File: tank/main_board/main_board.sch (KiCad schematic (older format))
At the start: 35 parts, among them J1 PowerOut, J10 PowerMotor, J11 SigOut, J12 Spk, J13 LEDs, J14 M0, J15 M1, J16 M2, J2 PowerIn, J3 Encoder0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

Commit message: fixes
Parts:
- removed U3: SN74HC595, custom:DIP-16_W7.62mm, symbol custom:SN74HC595-custom
- added U3: SN74HC595, custom:DIP-16_W7.62mm, symbol custom:SN74HC595
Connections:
- net 4.5V: now also U3.16 (VCC)
- net GND: now also U3.13 (G), U3.8 (GND)
- net M0+: now also U3.15 (QA)
- net M0-: now also U3.1 (QB)
- net M1+: now also U3.2 (QC)
- net M1-: now also U3.3 (QD)
- net M2+: now also U3.4 (QE)
- net M2-: now also U3.5 (QF)
- net SERIAL_CLOCK: now also U3.11 (SRCLK)
- net SERIAL_DATA: now also U3.14 (SER)
- net SERIAL_LATCH: now also U3.12 (RCLK)
- net at C8.1, D1.2 (A), R1.2: now also U3.10 (SRCLR)
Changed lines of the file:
@@
 	1    0    0    -1
-$EndComp
-$Comp
-L custom:PWR_FLAG-power #FLG02
-U 1 1 59E6BC0C
-P 1350 5550
-F 0 "#FLG02" H 1350 5625 50  0001 C CNN
-F 1 "PWR_FLAG" H 1350 5700 50  0000 C CNN
-F 2 "" H 1350 5550 50  0001 C CNN
-F 3 "" H 1350 5550 50  0001 C CNN
-	1    1350 5550
-	1    0    0    -1
-$EndComp
-$Comp
-L custom:PWR_FLAG-power #FLG01
-U 1 1 59E6BD3A
-P 1200 5650
-F 0 "#FLG01" H 1200 5725 50  0001 C CNN
-F 1 "PWR_FLAG" H 1200 5800 50  0000 C CNN
-F 2 "" H 1200 5650 50  0001 C CNN
-F 3 "" H 1200 5650 50  0001 C CNN
-	1    1200 5650
-	-1   0    0    1
 $EndComp
 NoConn ~ 2400 4350
@@
 Wire Wire Line
 	6000 3850 6000 4000
-Connection ~ 1350 5550
-Connection ~ 1200 5650
 Wire Wire Line
 	6450 3300 6450 3700
@@
 Text GLabel 6650 6475 2    60   Input ~ 0
 M2-
-$Comp
-L custom:SN74HC595-custom U3
-U 1 1 5A486ACA
-P 5950 6425
-F 0 "U3" H 6100 7025 50  0000 C CNN
-F 1 "SN74HC595" H 5950 5825 50  0000 C CNN
-F 2 "custom:DIP-16_W7.62mm" H 5950 6425 50  0001 C CNN
-F 3 "" H 5950 6425 50  0001 C CNN
-	1    5950 6425
-	1    0    0    -1
-$EndComp
 Text GLabel 4100 5800 0    60   Input ~ 0
 4.5V
@@
 	3250 4600 3250 4700
 Wire Wire Line
-	1350 5550 1500 5550
-Wire Wire Line
-	1200 5650 1350 5650
-Wire Wire Line
 	5900 3750 6700 3750
 Wire Wire Line
@@
 Wire Wire Line
 	2500 5550 2650 5550
-Wire Wire Line
-	1000 5650 1200 5650
 Wire Wire Line
 	5850 4400 5850 4550
@@
 Rx
 Wire Wire Line
-	3150 6850 3450 6850
+	3150 6850 3175 6850
 Text GLabel 3450 6850 2    50   Input ~ 0
 Vm
@@
 NoConn ~ 10075 -325
 NoConn ~ 9200 4575
-$Comp
-L custom:PWR_FLAG-power #FLG0101
-U 1 1 61D3DF25
-P 3150 6850
-F 0 "#FLG0101" H 3150 6925 50  0001 C CNN
-F 1 "PWR_FLAG" H 3150 7000 50  0000 C CNN
-F 2 "" H 3150 6850 50  0001 C CNN
-F 3 "" H 3150 6850 50  0001 C CNN
-	1    3150 6850
-	1    0    0    -1
-$EndComp
-Wire Wire Line
-	950  5550 1200 5550
-Wire Wire Line
-	1200 5550 1350 5550
+Wire Wire Line
+	950  5550 1075 5550
 Connection ~ 1200 5550
 Wire Wire Line
@@
 9V
 Wire Wire Line
-	3150 6950 3450 6950
+	3150 6950 3175 6950
 Wire Wire Line
 	2200 6150 2850 6150
-$Comp
-L custom:PWR_FLAG-power #FLG0102
-U 1 1 61D3D792
-P 3150 6950
-F 0 "#FLG0102" H 3150 7025 50  0001 C CNN
-F 1 "PWR_FLAG" H 3150 7123 50  0000 C CNN
-F 2 "" H 3150 6950 50  0001 C CNN
-F 3 "~" H 3150 6950 50  0001 C CNN
-	1    3150 6950
-	1    0    0    -1
-$EndComp
-Connection ~ 3150 6950
 Text GLabel 5250 6475 0    50   Input ~ 0
 SERIAL_LATCH
@@
 Text GLabel 5850 4400 2    50   Input ~ 0
 Bump1
+Wire Wire Line
+	1200 5550 1500 5550
+Wire Wire Line
+	1000 5650 1075 5650
+$Comp
+L custom:SN74HC595 U3
+U 1 1 6202E6D3
+P 5950 6425
+F 0 "U3" H 5950 7191 50  0000 C CNN
+F 1 "SN74HC595" H 5950 7100 50  0000 C CNN
+F 2 "custom:DIP-16_W7.62mm" H 5950 6425 50  0001 C CNN
+F 3 "" H 5950 6425 50  0001 C CNN
+	1    5950 6425
+	1    0    0    -1
+$EndComp
+$Comp
+L custom:PWR_FLAG #FLG0101
+U 1 1 62037CB6
+P 1075 5550
+F 0 "#FLG0101" H 1075 5625 50  0001 C CNN
+F 1 "PWR_FLAG" H 1075 5723 50  0000 C CNN
+F 2 "" H 1075 5550 50  0001 C CNN
+F 3 "" H 1075 5550 50  0001 C CNN
+	1    1075 5550
+	1    0    0    -1
+$EndComp
+Connection ~ 1075 5550
+Wire Wire Line
+	1075 5550 1200 5550
+$Comp
+L custom:PWR_FLAG #FLG0102
+U 1 1 62038348
+P 1075 5650
+F 0 "#FLG0102" H 1075 5725 50  0001 C CNN
+F 1 "PWR_FLAG" H 1075 5823 50  0000 C CNN
+F 2 "" H 1075 5650 50  0001 C CNN
+F 3 "" H 1075 5650 50  0001 C CNN
+	1    1075 5650
+	-1   0    0    1
+$EndComp
+Connection ~ 1075 5650
+Wire Wire Line
+	1075 5650 1350 5650
+$Comp
+L custom:PWR_FLAG #FLG0103
+U 1 1 620389A9
+P 3175 6850
+F 0 "#FLG0103" H 3175 6925 50  0001 C CNN
+F 1 "PWR_FLAG" H 3175 7023 50  0000 C CNN
+F 2 "" H 3175 6850 50  0001 C CNN
+F 3 "" H 3175 6850 50  0001 C CNN
+	1    3175 6850
+	1    0    0    -1
+$EndComp
+Connection ~ 3175 6850
+Wire Wire Line
+	3175 6850 3450 6850
+$Comp
+L custom:PWR_FLAG #FLG0104
+U 1 1 62038DED
+P 3175 6950
+F 0 "#FLG0104" H 3175 7025 50  0001 C CNN
+F 1 "PWR_FLAG" H 3175 7123 50  0000 C CNN
+F 2 "" H 3175 6950 50  0001 C CNN
+F 3 "" H 3175 6950 50  0001 C CNN
+	1    3175 6950
+	-1   0    0    1
+$EndComp
+Connection ~ 3175 6950
+Wire Wire Line
+	3175 6950 3450 6950
 $EndSCHEMATC

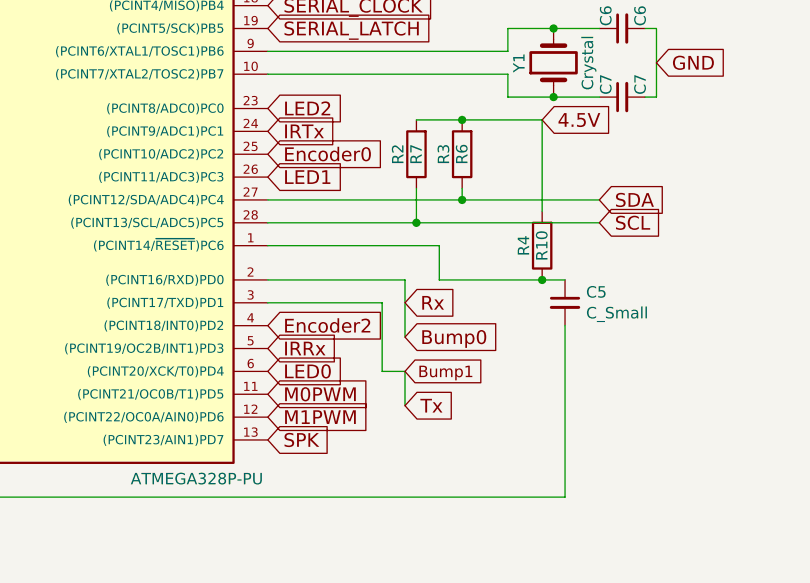
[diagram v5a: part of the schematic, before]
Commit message: Version 0.11: - Better labelling - Put LED output on Rx and Tx pins. This way, we won't be attaching interrutps to Serial pins
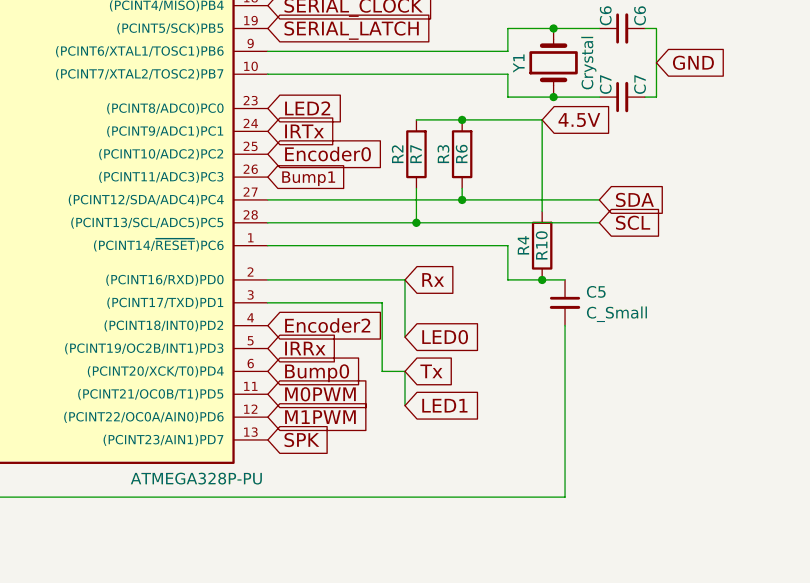
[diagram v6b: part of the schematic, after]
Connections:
- net Bump0: now also U2.6 ((PCINT20/XCK/T0)PD4); no longer J9.4 (Pin_4), U2.2 ((PCINT16/RXD)PD0)
- net Bump1: now also U2.26 ((PCINT11/ADC3)PC3); no longer J9.5 (Pin_5), U2.3 ((PCINT17/TXD)PD1)
- net LED0: now also J9.4 (Pin_4), U2.2 ((PCINT16/RXD)PD0); no longer U2.6 ((PCINT20/XCK/T0)PD4)
- net LED1: now also J9.5 (Pin_5), U2.3 ((PCINT17/TXD)PD1); no longer U2.26 ((PCINT11/ADC3)PC3)
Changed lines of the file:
@@
 Connection ~ 3250 4600
-Wire Wire Line
-	5250 3850 6000 3850
-Wire Wire Line
-	6000 4000 6450 4000
-Wire Wire Line
-	6000 3850 6000 4000
 Wire Wire Line
 	6450 3300 6450 3700
@@
 Text GLabel 2050 3500 2    60   Input ~ 0
 GND
-Text GLabel 5250 4400 2    60   Input ~ 0
+Text GLabel 5850 4250 2    60   Input ~ 0
 LED0
-Text GLabel 5250 3550 2    60   Input ~ 0
+Text GLabel 5850 4550 2    60   Input ~ 0
 LED1
 Text GLabel 6450 3300 2    60   Input ~ 0
@@
 Text GLabel 6950 3050 2    60   Input ~ 0
 GND
-Connection ~ 6450 4000
 Text GLabel 3150 950  0    60   Input ~ 0
 IRTx
@@
 Wire Wire Line
 	5750 4400 5850 4400
-Text GLabel 5850 4250 2    60   Input ~ 0
+Text GLabel 5250 4400 2    60   Input ~ 0
 Bump0
 Text GLabel 5500 1800 0    60   Input ~ 0
@@
 Wire Wire Line
 	5850 4400 5850 4550
-Text GLabel 5850 4550 2    60   Input ~ 0
+Text GLabel 5850 4400 2    60   Input ~ 0
 Tx
-Text GLabel 5850 4100 2    60   Input ~ 0
+Text GLabel 5850 4000 2    60   Input ~ 0
 Rx
 Wire Wire Line
@@
 Wire Wire Line
 	5250 7050 5650 7050
-Text GLabel 5850 4400 2    50   Input ~ 0
+Text GLabel 5250 3550 2    50   Input ~ 0
 Bump1
 Wire Wire Line
@@
 Wire Wire Line
 	3175 6950 3450 6950
+Wire Wire Line
+	6450 4000 6300 4000
+Wire Wire Line
+	6300 4000 6300 3850
+Wire Wire Line
+	5250 3850 6300 3850
+Connection ~ 6450 4000
 $EndSCHEMATC
